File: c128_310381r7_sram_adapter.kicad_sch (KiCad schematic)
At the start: 4 parts, among them U1 128K x 8 SRAM, U2 74HCT32, U3 74HCT08, U4 74HCT573

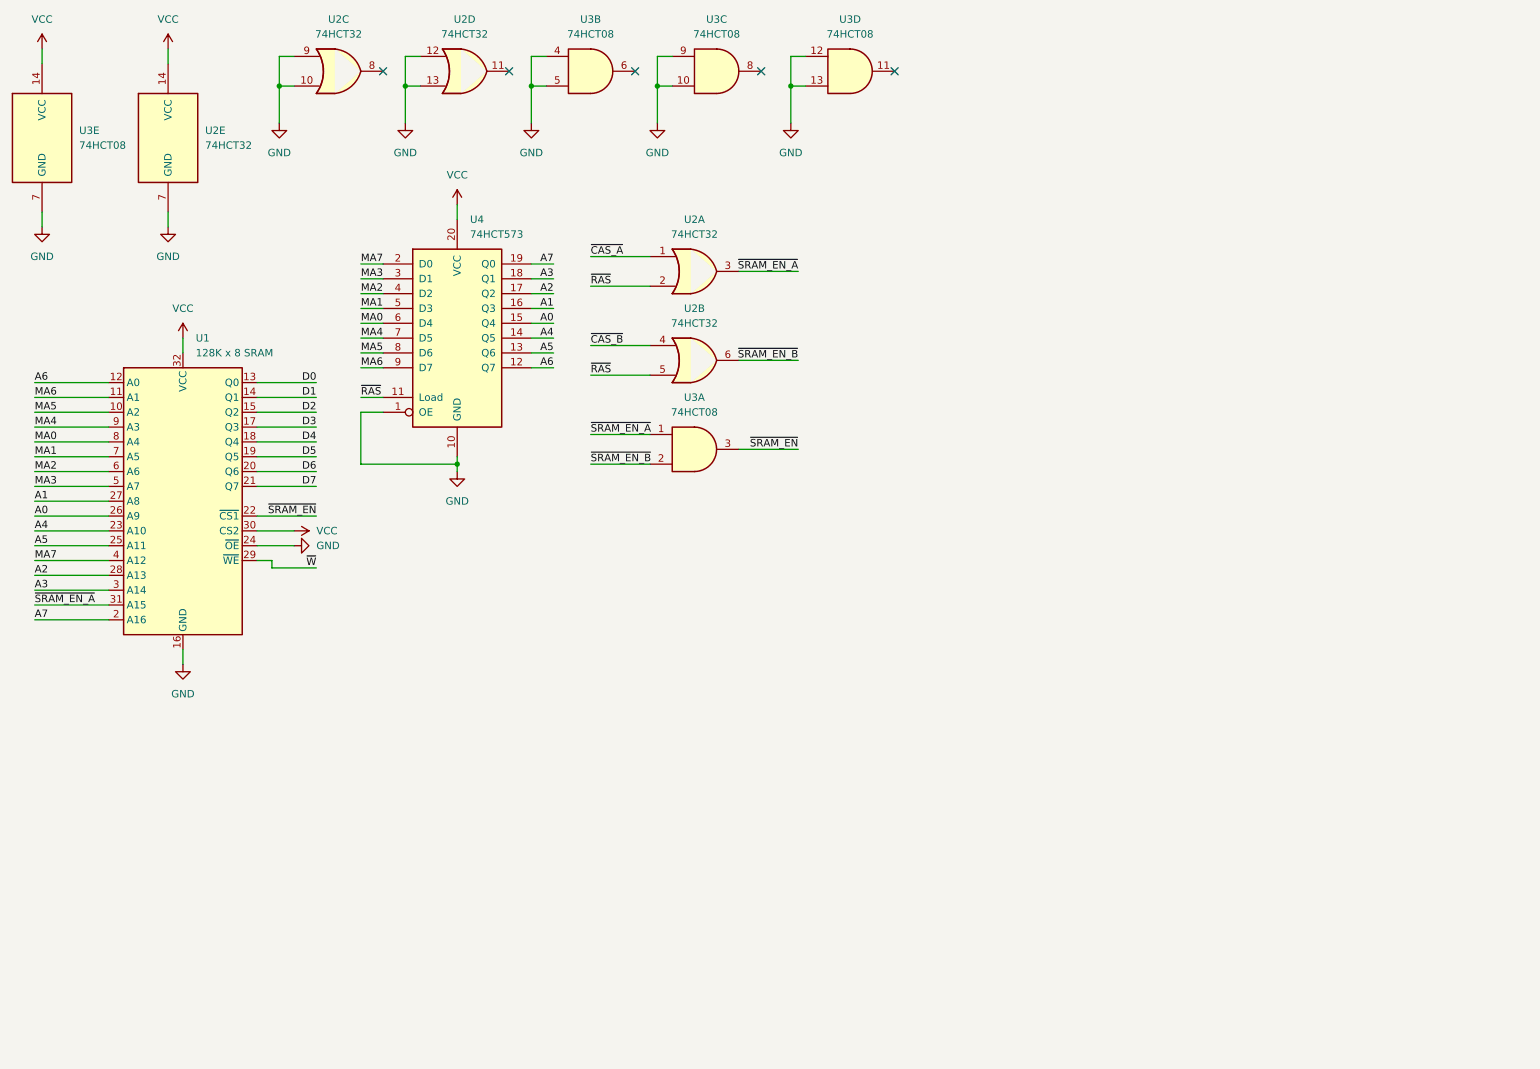
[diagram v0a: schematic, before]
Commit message: Schematic for the connections of the SRAM adapter
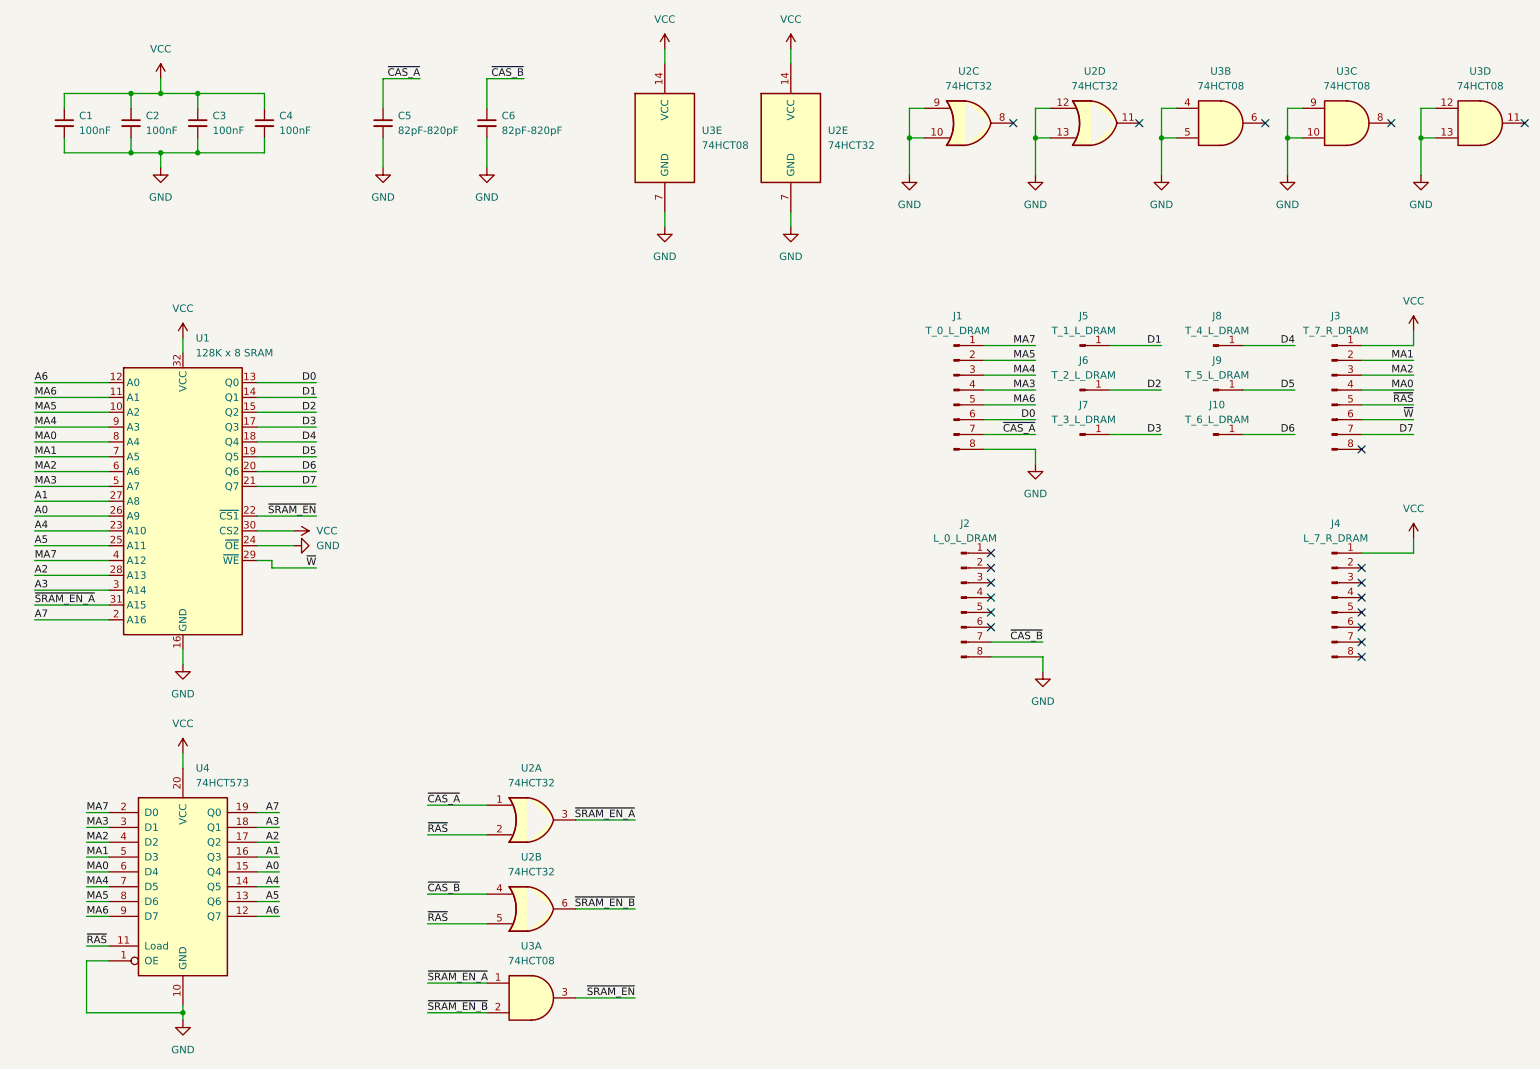
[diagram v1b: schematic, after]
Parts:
- added C1, C2, C3, C4: 100nF, Capacitor_SMD:C_1206_3216Metric_Pad1.33x1.80mm_HandSolder, symbol Device:C_Small
- added C5, C6: 82pF-820pF, Capacitor_SMD:C_1206_3216Metric_Pad1.33x1.80mm_HandSolder, symbol Device:C_Small
- added J1: T_0_L_DRAM, Connector_PinHeader_2.54mm:PinHeader_1x08_P2.54mm_Vertical, symbol Connector:Conn_01x08_Pin
- added J10: T_6_L_DRAM, Connector_PinHeader_2.54mm:PinHeader_1x01_P2.54mm_Vertical, symbol Connector:Conn_01x01_Pin
- added J2: L_0_L_DRAM, Connector_PinHeader_2.54mm:PinHeader_1x08_P2.54mm_Vertical, symbol Connector:Conn_01x08_Pin
- added J3: T_7_R_DRAM, Connector_PinHeader_2.54mm:PinHeader_1x08_P2.54mm_Vertical, symbol Connector:Conn_01x08_Pin
- added J4: L_7_R_DRAM, Connector_PinHeader_2.54mm:PinHeader_1x08_P2.54mm_Vertical, symbol Connector:Conn_01x08_Pin
- added J5: T_1_L_DRAM, Connector_PinHeader_2.54mm:PinHeader_1x01_P2.54mm_Vertical, symbol Connector:Conn_01x01_Pin
- added J6: T_2_L_DRAM, Connector_PinHeader_2.54mm:PinHeader_1x01_P2.54mm_Vertical, symbol Connector:Conn_01x01_Pin
- added J7: T_3_L_DRAM, Connector_PinHeader_2.54mm:PinHeader_1x01_P2.54mm_Vertical, symbol Connector:Conn_01x01_Pin
- added J8: T_4_L_DRAM, Connector_PinHeader_2.54mm:PinHeader_1x01_P2.54mm_Vertical, symbol Connector:Conn_01x01_Pin
- added J9: T_5_L_DRAM, Connector_PinHeader_2.54mm:PinHeader_1x01_P2.54mm_Vertical, symbol Connector:Conn_01x01_Pin
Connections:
- net D0: now also J1.6 (Pin_6)
- net D1: now also J5.1 (Pin_1)
- net D2: now also J6.1 (Pin_1)
- net D3: now also J7.1 (Pin_1)
- net D4: now also J8.1 (Pin_1)
- net D5: now also J9.1 (Pin_1)
- net D6: now also J10.1 (Pin_1)
- net D7: now also J3.7 (Pin_7)
- net GND: now also C1.2, C2.2, C3.2, C4.2, C5.2, C6.2, J1.8 (Pin_8), J2.8 (Pin_8)
- net MA0: now also J3.4 (Pin_4)
- net MA1: now also J3.2 (Pin_2)
- net MA2: now also J3.3 (Pin_3)
- net MA3: now also J1.4 (Pin_4)
- net MA4: now also J1.3 (Pin_3)
- net MA5: now also J1.2 (Pin_2)
- net MA6: now also J1.5 (Pin_5)
- net MA7: now also J1.1 (Pin_1)
- net VCC: now also C1.1, C2.1, C3.1, C4.1, J3.1 (Pin_1), J4.1 (Pin_1)
- net ~{CAS_A}: now also C5.1, J1.7 (Pin_7)
- net ~{CAS_B}: now also C6.1, J2.7 (Pin_7)
- net ~{RAS}: now also J3.5 (Pin_5)
- net ~{W}: now also J3.6 (Pin_6)
- no-connect marks 5 -> 19
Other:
- moved on the sheet: U2A, U2B, U2C, U2D, U2E, U3A, U3B, U3C, U3D, U3E, U4

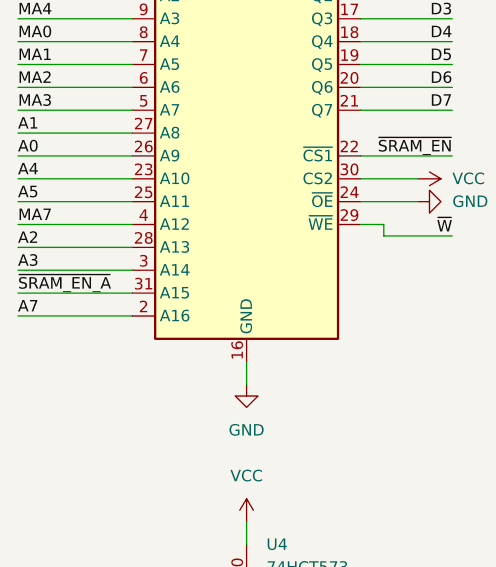
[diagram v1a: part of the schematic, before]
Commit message: Wire A15 to /CAS_A signal
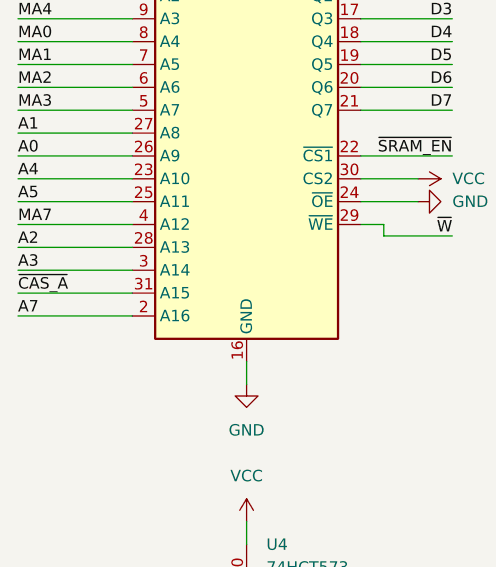
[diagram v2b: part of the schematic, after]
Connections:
- net ~{CAS_A}: now also U1.31 (A15)
- net ~{SRAM_EN_A}: no longer U1.31 (A15)
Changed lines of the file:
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@@
 		)
 	)
-	(label "~{SRAM_EN_A}"
+	(label "~{CAS_A}"
 		(at 19.05 115.57 0)
 		(effects

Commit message: Add custom footprints for components in this adapter
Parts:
- C1, C2, C3, C4: footprint Capacitor_SMD:C_1206_3216Metric_Pad1.33x1.80mm_HandSolder -> DoubleFootprint_Library:C_Disc_1206_P5.00mm
- C5, C6: footprint Capacitor_SMD:C_1206_3216Metric_Pad1.33x1.80mm_HandSolder -> DoubleFootprint_Library:C_Disc_1206_P2.50mm
- U1: footprint Package_DIP:DIP-32_W15.24mm -> DoubleFootprint_Library:DIP-SOP-32
- U2, U3: footprint Package_DIP:DIP-14_W7.62mm -> DoubleFootprint_Library:DIP-SO-14
- U4: footprint Package_DIP:DIP-20_W7.62mm -> DoubleFootprint_Library:DIP-TSSOP-20
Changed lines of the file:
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@@
 			)
 		)
-		(property "Footprint" "Capacitor_SMD:C_1206_3216Metric_Pad1.33x1.80mm_HandSolder"
+		(property "Footprint" "DoubleFootprint_Library:C_Disc_1206_P5.00mm"
 			(at 35.56 33.02 0)
 			(effects
@@
 			)
 		)
-		(property "Footprint" "Capacitor_SMD:C_1206_3216Metric_Pad1.33x1.80mm_HandSolder"
+		(property "Footprint" "DoubleFootprint_Library:C_Disc_1206_P5.00mm"
 			(at 46.99 33.02 0)
 			(effects
@@
 			)
 		)
-		(property "Footprint" "Package_DIP:DIP-14_W7.62mm"
+		(property "Footprint" "DoubleFootprint_Library:DIP-SO-14"
 			(at 104.14 167.64 0)
 			(effects
@@
 			)
 		)
-		(property "Footprint" "Package_DIP:DIP-14_W7.62mm"
+		(property "Footprint" "DoubleFootprint_Library:DIP-SO-14"
 			(at 222.25 33.02 0)
 			(effects
@@
 			)
 		)
-		(property "Footprint" "Package_DIP:DIP-14_W7.62mm"
+		(property "Footprint" "DoubleFootprint_Library:DIP-SO-14"
 			(at 266.7 33.02 0)
 			(effects
@@
 			)
 		)
-		(property "Footprint" "Capacitor_SMD:C_1206_3216Metric_Pad1.33x1.80mm_HandSolder"
+		(property "Footprint" "DoubleFootprint_Library:C_Disc_1206_P2.50mm"
 			(at 78.74 33.02 0)
 			(effects
@@
 			)
 		)
-		(property "Footprint" "Package_DIP:DIP-32_W15.24mm"
+		(property "Footprint" "DoubleFootprint_Library:DIP-SOP-32"
 			(at 44.45 97.79 0)
 			(effects
@@
 			)
 		)
-		(property "Footprint" "Package_DIP:DIP-20_W7.62mm"
+		(property "Footprint" "DoubleFootprint_Library:DIP-TSSOP-20"
 			(at 44.45 163.83 0)
 			(effects
@@
 			)
 		)
-		(property "Footprint" "Capacitor_SMD:C_1206_3216Metric_Pad1.33x1.80mm_HandSolder"
+		(property "Footprint" "DoubleFootprint_Library:C_Disc_1206_P5.00mm"
 			(at 58.42 33.02 0)
 			(effects
@@
 			)
 		)
-		(property "Footprint" "Package_DIP:DIP-14_W7.62mm"
+		(property "Footprint" "DoubleFootprint_Library:DIP-SO-14"
 			(at 179.07 33.02 0)
 			(effects
@@
 			)
 		)
-		(property "Footprint" "Package_DIP:DIP-14_W7.62mm"
+		(property "Footprint" "DoubleFootprint_Library:DIP-SO-14"
 			(at 148.59 35.56 0)
 			(effects
@@
 			)
 		)
-		(property "Footprint" "Capacitor_SMD:C_1206_3216Metric_Pad1.33x1.80mm_HandSolder"
+		(property "Footprint" "DoubleFootprint_Library:C_Disc_1206_P2.50mm"
 			(at 96.52 33.02 0)
 			(effects
@@
 			)
 		)
-		(property "Footprint" "Package_DIP:DIP-14_W7.62mm"
+		(property "Footprint" "DoubleFootprint_Library:DIP-SO-14"
 			(at 127 35.56 0)
 			(effects
@@
 			)
 		)
-		(property "Footprint" "Capacitor_SMD:C_1206_3216Metric_Pad1.33x1.80mm_HandSolder"
+		(property "Footprint" "DoubleFootprint_Library:C_Disc_1206_P5.00mm"
 			(at 24.13 33.02 0)
 			(effects
@@
 			)
 		)
-		(property "Footprint" "Package_DIP:DIP-14_W7.62mm"
+		(property "Footprint" "DoubleFootprint_Library:DIP-SO-14"
 			(at 243.84 33.02 0)
 			(effects
@@
 			)
 		)
-		(property "Footprint" "Package_DIP:DIP-14_W7.62mm"
+		(property "Footprint" "DoubleFootprint_Library:DIP-SO-14"
 			(at 200.66 33.02 0)
 			(effects
@@
 			)
 		)
-		(property "Footprint" "Package_DIP:DIP-14_W7.62mm"
+		(property "Footprint" "DoubleFootprint_Library:DIP-SO-14"
 			(at 104.14 152.4 0)
 			(effects
@@
 			)
 		)
-		(property "Footprint" "Package_DIP:DIP-14_W7.62mm"
+		(property "Footprint" "DoubleFootprint_Library:DIP-SO-14"
 			(at 104.14 182.88 0)
 			(effects
